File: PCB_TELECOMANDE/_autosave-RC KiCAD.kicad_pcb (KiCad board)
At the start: 2 copper layers, 29 parts, among them J1 USB4085, Q1 PMV45EN2, U3 ESP32-S3-WROOM-2-N32R8V, U4 TLV75801PDBV

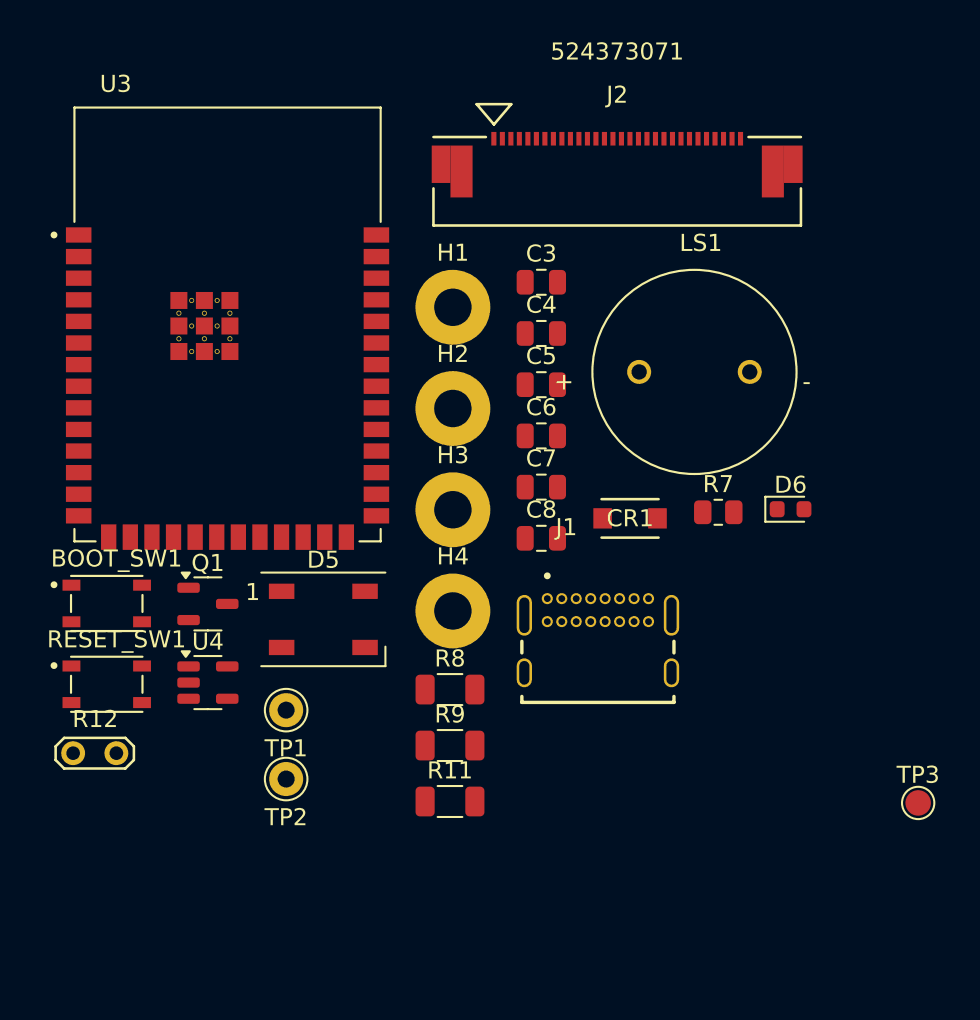
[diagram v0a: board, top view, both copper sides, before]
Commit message: Filesys Reorg + PD Negociator schematics
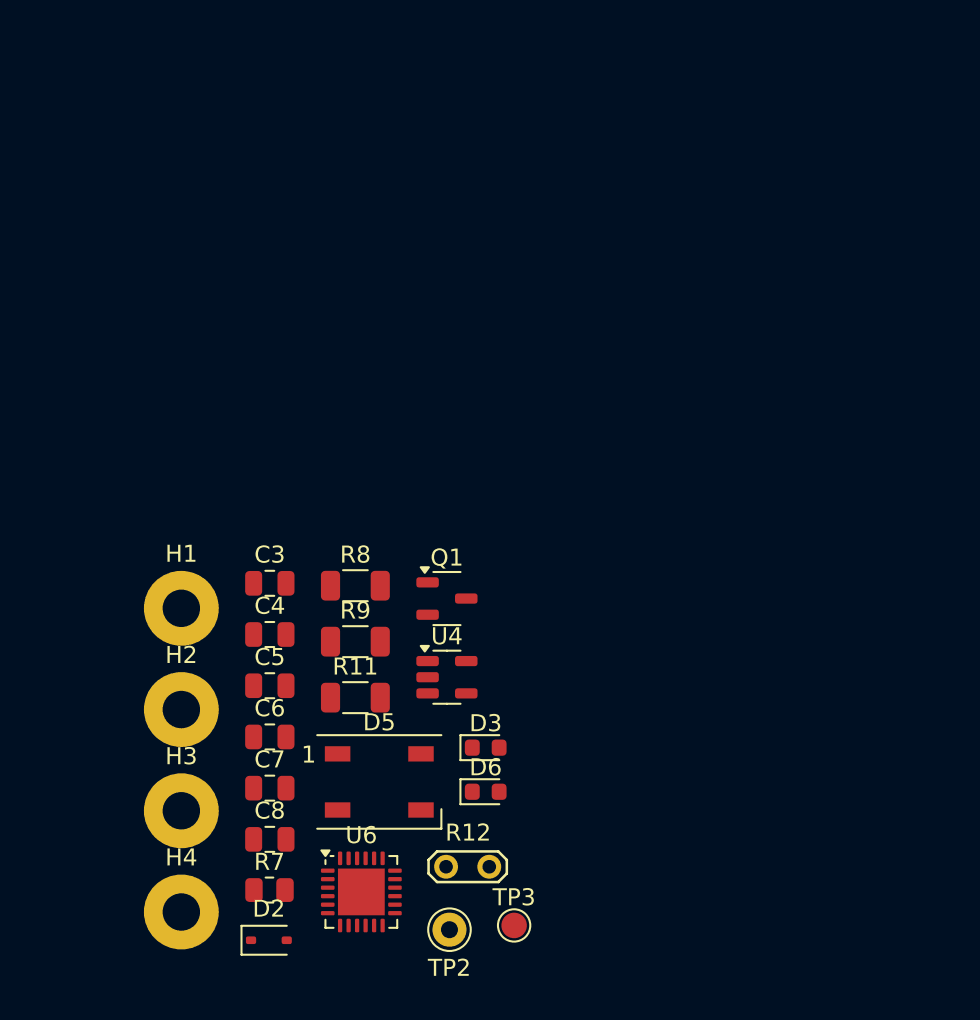
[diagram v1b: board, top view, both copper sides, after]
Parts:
- removed BOOT_SW1, RESET_SW1: PTS810_SJM_250_SMTR_LFS, Footprints:SW_PTS810_SJM_250_SMTR_LFS
- removed CR1: SMF9.0CA, Footprints:SOD-123F_LTF
- removed J1: USB4085, Footprints:GCT_USB4085-GF-A_REVB
- removed J2: ~, Footprints:CON_524373071_MOL
- removed LS1: CEM-1206S, Footprints:CUI_CEM-1206S
- removed TP1: GND, Connector_Pin:Pin_D1.0mm_L10.0mm
- removed U3: ESP32-S3-WROOM-2-N32R8V, Footprints:XCVR_ESP32-S3-WROOM-2-N32R8V
- added D2: BAT60A, Diode_SMD:D_SOD-323, F.Cu at (73.2, 96.0)
- added D3: LED, LED_SMD:LED_0603_1608Metric, F.Cu at (85.9, 84.7)
- added U6: CYPD3177-24LQ, Package_DFN_QFN:QFN-24-1EP_4x4mm_P0.5mm_EP2.75x2.75mm, F.Cu at (78.6, 93.2)
- moved R7 34.5 mm to (73.2, 93.1)
- moved TP3 24.8 mm to (87.6, 95.2)
- moved D6 24.4 mm to (85.9, 87.3)
- moved C3 23.8 mm to (73.2, 75.0)
- moved C8 23.8 mm to (73.2, 90.1)
- moved C4 23.8 mm to (73.2, 78.0)
- moved C5 23.8 mm to (73.2, 81.1)
- moved C6 23.8 mm to (73.2, 84.1)
- moved C7 23.8 mm to (73.2, 87.1)
- moved H1 23.8 mm to (68.0, 76.5)
- moved H2 23.8 mm to (68.0, 82.5)
- moved H3 23.8 mm to (68.0, 88.4)
- moved H4 23.8 mm to (68.0, 94.4)
- moved R12 22.9 mm to (83.6, 91.7)
- moved Q1 14.1 mm to (83.7, 75.9)
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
